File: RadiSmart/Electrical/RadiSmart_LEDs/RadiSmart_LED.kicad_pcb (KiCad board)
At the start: 2 copper layers, 199.4 x 17.8 mm, 16 parts, among them P1 CONN_01X02, P2 CONN_01X02

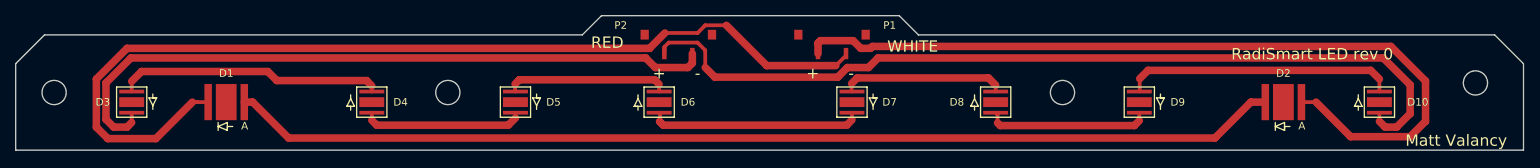
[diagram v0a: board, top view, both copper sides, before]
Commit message: chunked up traces on led board and generated new gerbers
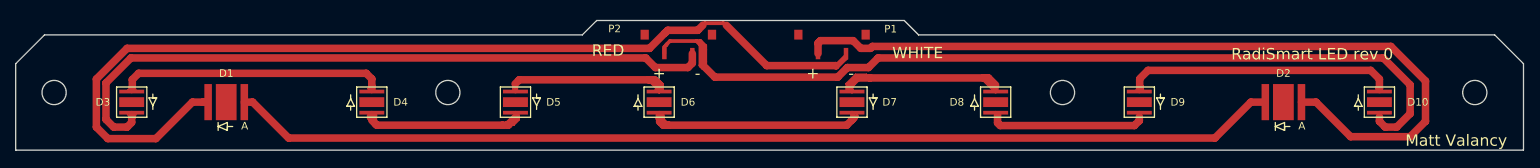
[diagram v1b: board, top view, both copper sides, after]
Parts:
- moved REF** 1.35 mm to (234.9, 62.3)
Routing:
- net Net-(D7-Pad2): track 21.7 -> 36.9 mm
- net Net-(D10-Pad2): track 115.6 -> 125.0 mm
- net Net-(D4-Pad2): track 21.4 -> 30.3 mm
- net Net-(D5-Pad2): track 21.5 -> 28.4 mm
- net Net-(D6-Pad2): track 28.2 -> 34.8 mm
- net Net-(D3-Pad2): track 35.2 -> 40.3 mm
- net Net-(D1-Pad1): track 128.9 -> 131.9 mm
- net Net-(D10-Pad1): track 36.0 -> 38.3 mm
- net Net-(D3-Pad1): track 91.1 -> 92.6 mm
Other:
- board size 199.4 x 17.8 mm -> 199.4 x 17.1 mm
